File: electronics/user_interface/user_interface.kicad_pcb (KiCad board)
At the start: 2 copper layers, 2 parts

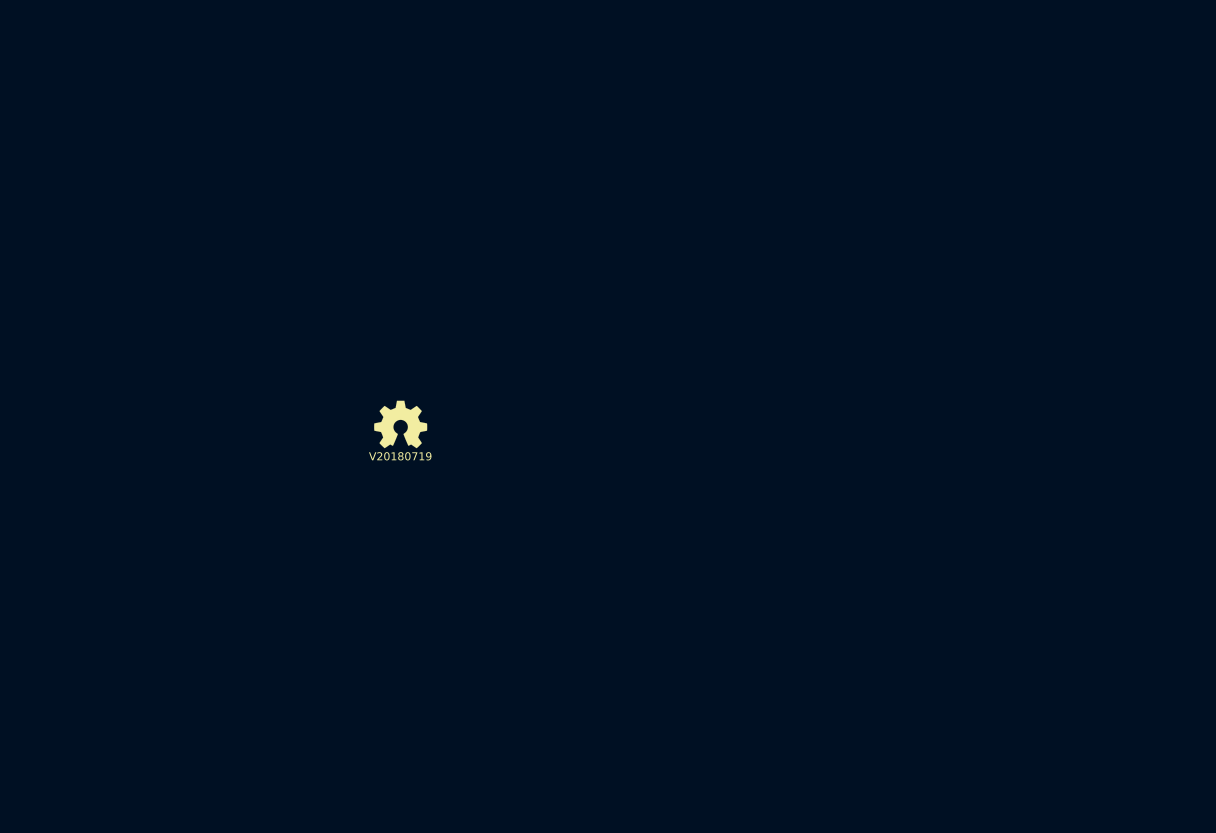
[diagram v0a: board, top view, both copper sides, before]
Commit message: board outline, input circuit layout
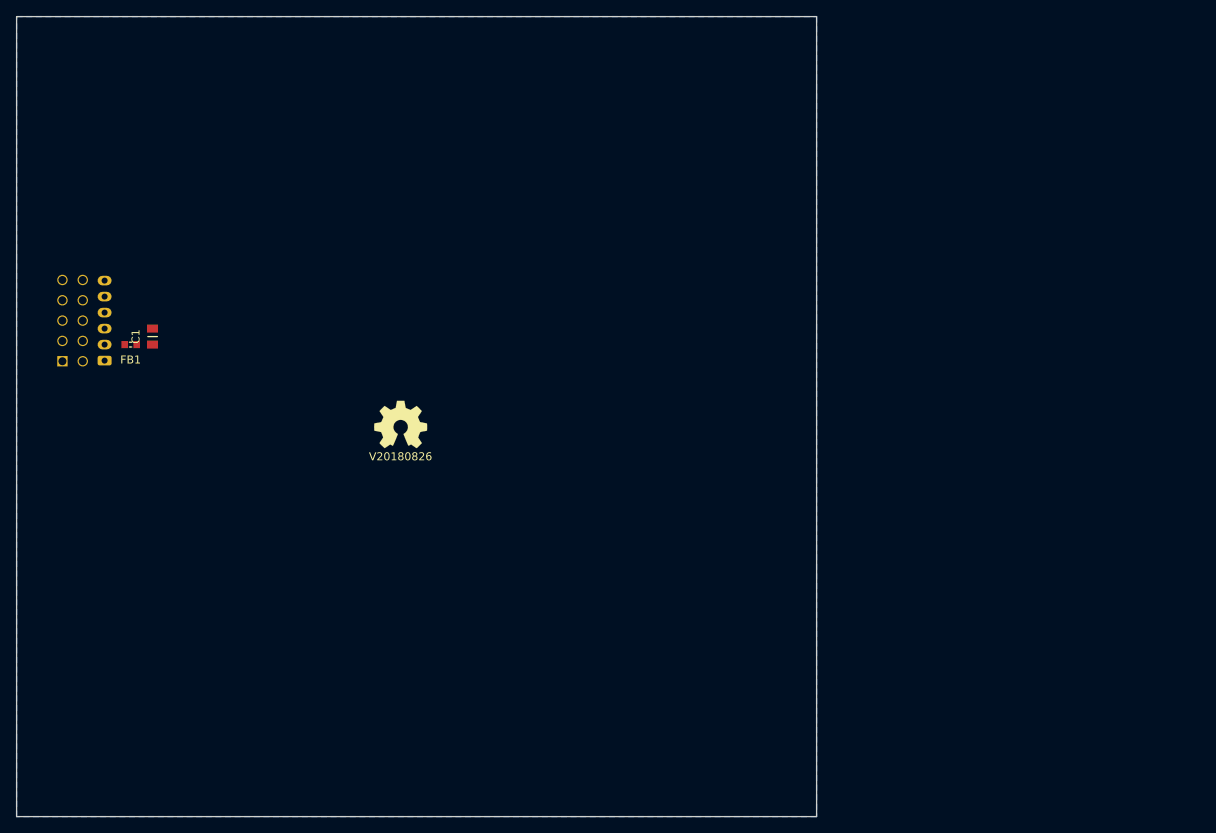
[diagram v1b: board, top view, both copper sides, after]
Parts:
- added C1: 10u, SquantorRcl:C_0805, F.Cu at (117.0, 90.0)
- added FB1: 600, SquantorRcl:L_0603, F.Cu at (114.2, 91.0)
- added J1: Conn_01x06, Connector_JST:JST_PH_S6B-PH-K_1x06_P2.00mm_Horizontal, B.Cu at (111.0, 93.0)
- added J2: Conn_02x05_Odd_Even, SquantorConnectors:Header-0254-2X05-H010, B.Cu at (107.0, 88.0)
- N2: value V20180719 -> V20180826
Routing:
- added copper zone on B.Cu, net /VSS
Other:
- board outline added: 100 x 100 mm

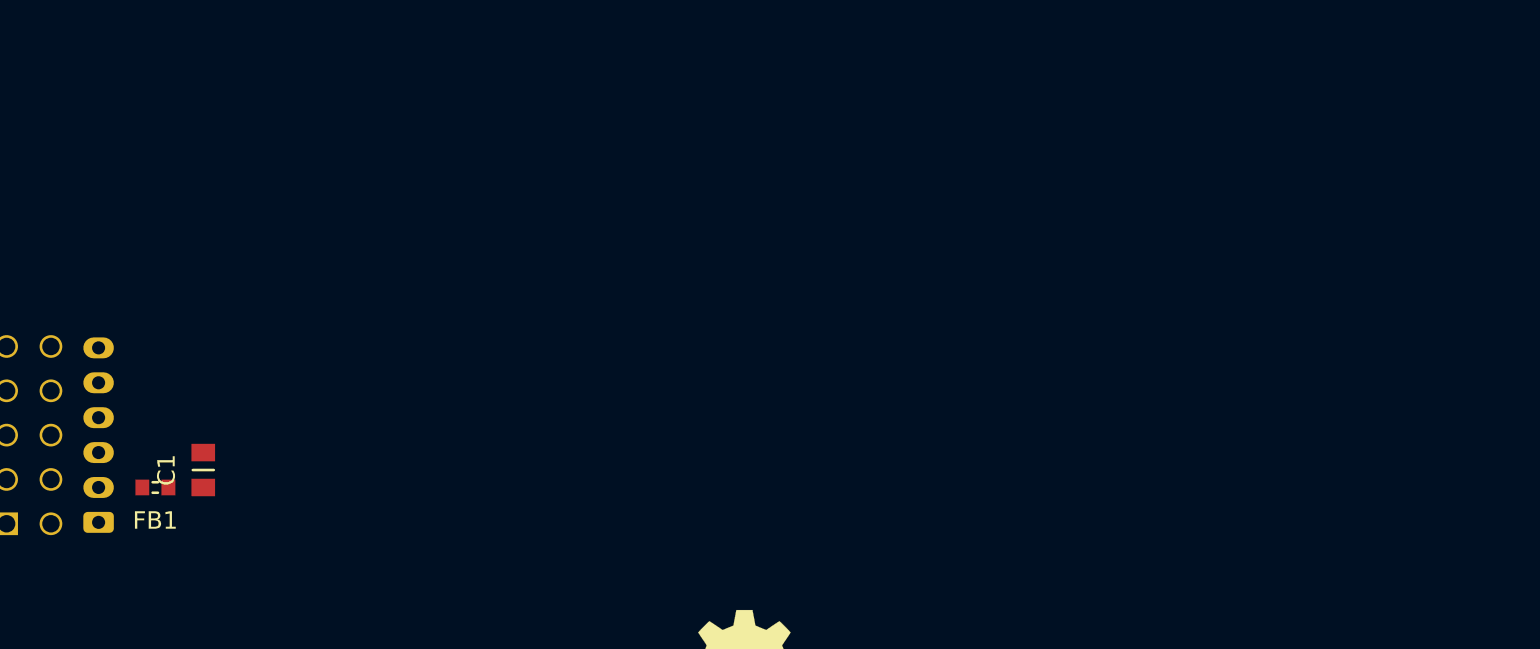
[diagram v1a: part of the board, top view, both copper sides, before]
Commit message: footprints assignment, minor layout positioning
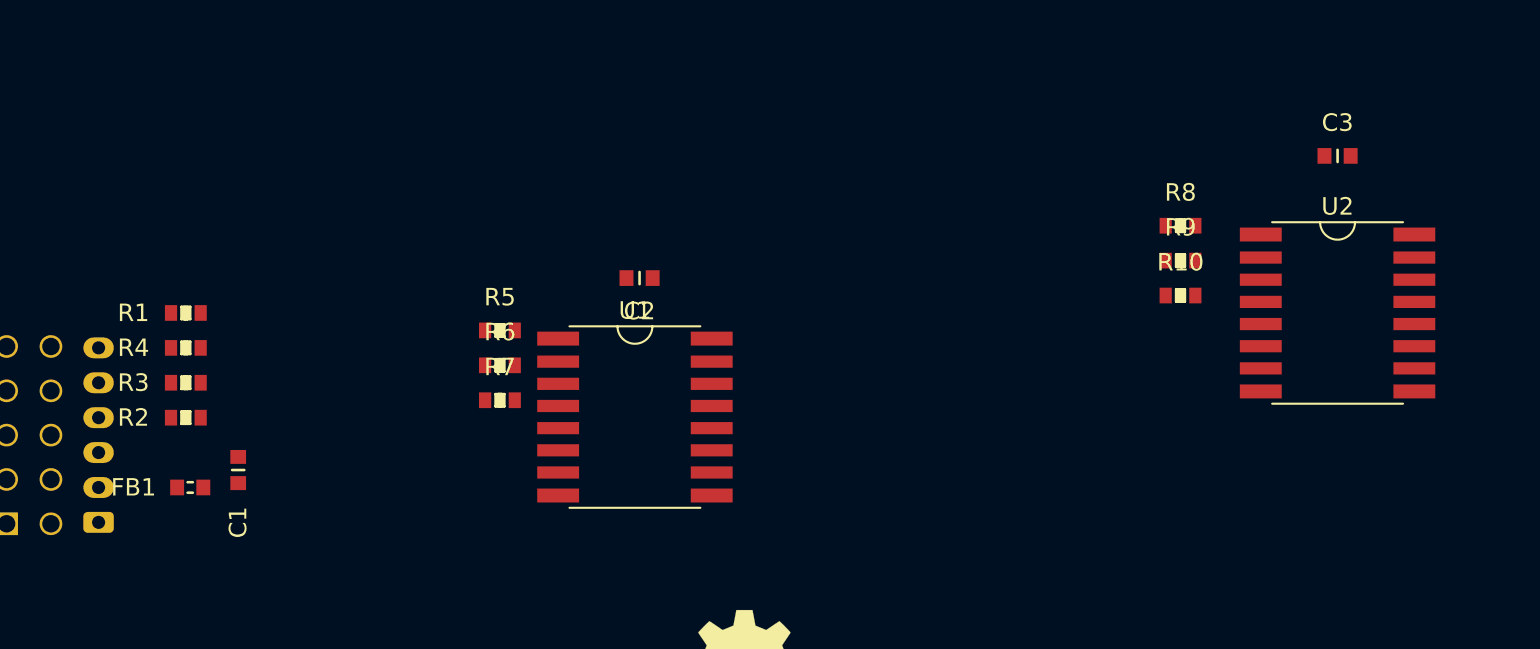
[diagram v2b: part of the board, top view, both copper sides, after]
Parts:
- added C2: 1u, SquantorRcl:C_0603, F.Cu at (142.0, 79.0)
- added C3: 1u, SquantorRcl:C_0603, F.Cu at (182.0, 72.0)
- added R1: 4.7K, SquantorRcl:R_0603_hand, F.Cu at (116.0, 81.0)
- added R10: 4.7K, SquantorRcl:R_0603_hand, F.Cu at (173.0, 80.0)
- added R2: 100, SquantorRcl:R_0603_hand, F.Cu at (116.0, 87.0)
- added R3: 100, SquantorRcl:R_0603_hand, F.Cu at (116.0, 85.0)
- added R4: 100, SquantorRcl:R_0603_hand, F.Cu at (116.0, 83.0)
- added R5: 4.7K, SquantorRcl:R_0603_hand, F.Cu at (134.0, 82.0)
- added R6: 4.7K, SquantorRcl:R_0603_hand, F.Cu at (134.0, 84.0)
- added R7: 4.7K, SquantorRcl:R_0603_hand, F.Cu at (134.0, 86.0)
- added R8: 4.7K, SquantorRcl:R_0603_hand, F.Cu at (173.0, 76.0)
- added R9: 4.7K, SquantorRcl:R_0603_hand, F.Cu at (173.0, 78.0)
- added U1: PCF8574, SquantorIC:SOT162-1-NXP, F.Cu at (141.7, 87.0)
- added U2: PCF8574, SquantorIC:SOT162-1-NXP, F.Cu at (182.0, 81.0)
- C1: footprint SquantorRcl:C_0805 -> SquantorRcl:C_0603
- moved C1 2.00 mm to (119.0, 90.0)
- moved FB1 2.00 mm to (116.2, 91.0)
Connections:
- net /!INT renamed /!INT_RAW
- net /SCL renamed /SCL_RAW
- net /SDA renamed /SDA_RAW

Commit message: updated date
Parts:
- N2: value V20180826 -> V20200514
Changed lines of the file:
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@@
       (effects (font (size 1 1) (thickness 0.15)))
     )
-    (fp_text value V20180826 (at 0 0) (layer F.SilkS)
+    (fp_text value V20200514 (at 0 0) (layer F.SilkS)
       (effects (font (size 1 1) (thickness 0.15)))
     )

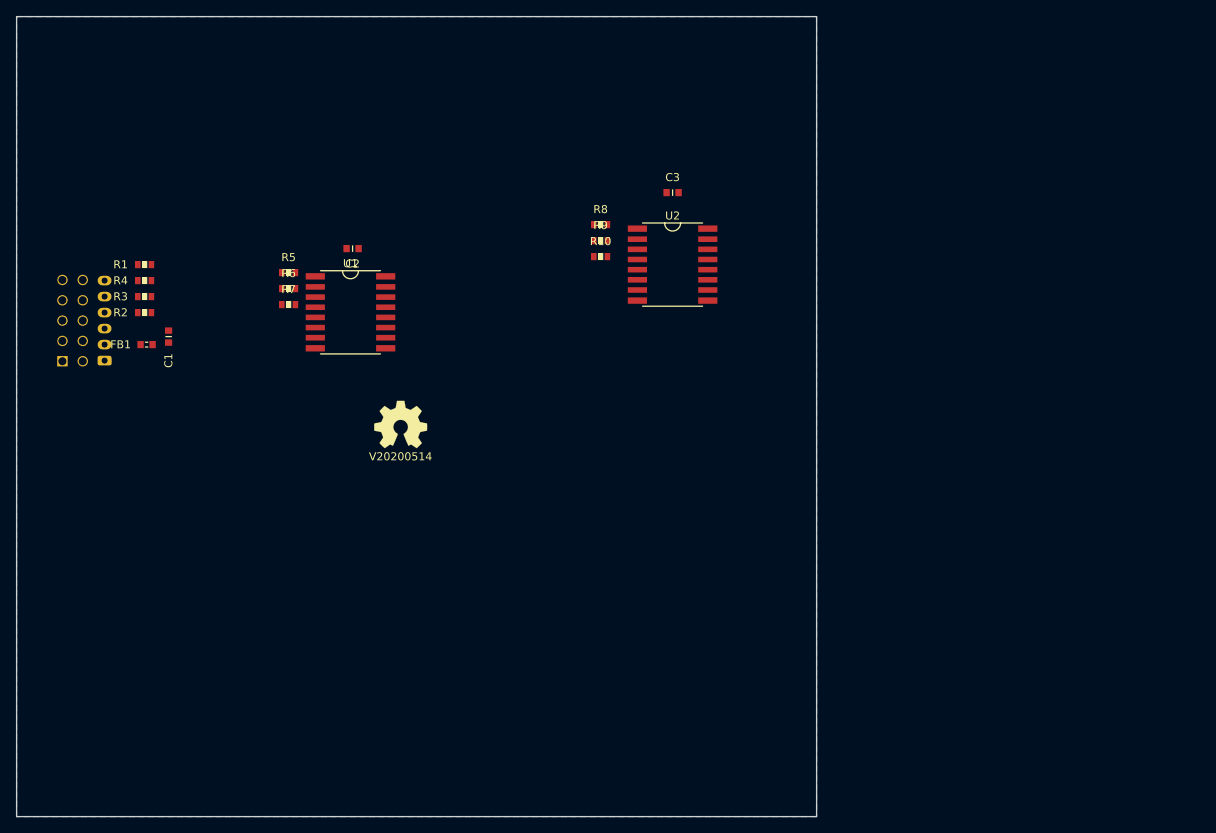
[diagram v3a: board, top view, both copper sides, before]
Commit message: added mounting holes, some silk moves
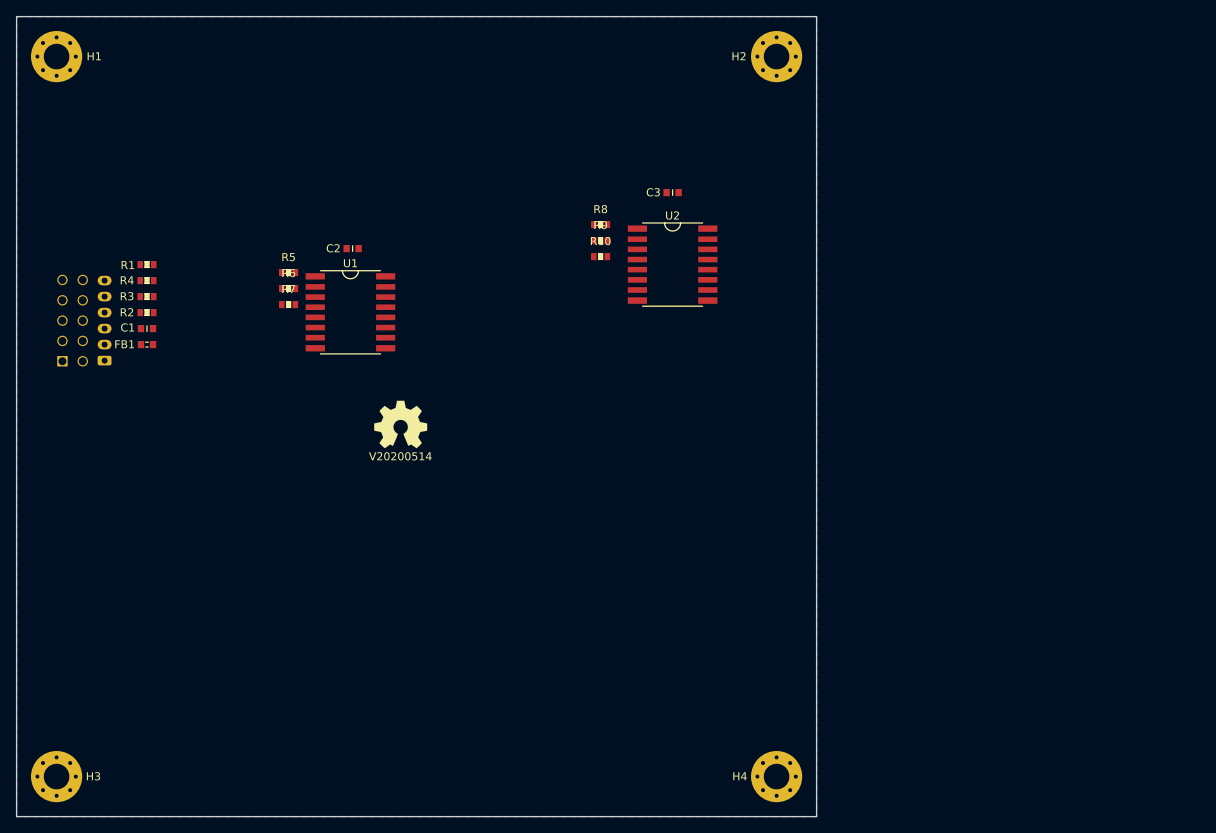
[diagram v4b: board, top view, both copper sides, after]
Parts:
- added H1: M3, MountingHole:MountingHole_3.2mm_M3_Pad_Via, F.Cu at (105.0, 55.0)
- added H2: M3, MountingHole:MountingHole_3.2mm_M3_Pad_Via, F.Cu at (195.0, 55.0)
- added H3: M3, MountingHole:MountingHole_3.2mm_M3_Pad_Via, F.Cu at (105.0, 145.0)
- added H4: M3, MountingHole:MountingHole_3.2mm_M3_Pad_Via, F.Cu at (195.0, 145.0)
- moved C1 2.88 mm to (116.3, 89.0), turned to 180 degrees
- moved R1 0.30 mm to (116.3, 81.0)
- moved R2 0.30 mm to (116.3, 87.0)
- moved R3 0.30 mm to (116.3, 85.0)
- moved R4 0.30 mm to (116.3, 83.0)

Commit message: added 3 switches extra to schematic
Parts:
- added C4: 1u, SquantorRcl:C_0603, F.Cu at (134.2, 114.4)
- added D1: RB521S-30, SquantorDiodes:SOD-523, F.Cu at (129.9, 119.4)
- added R11: TBD, SquantorRcl:R_0603_hand, F.Cu at (130.3, 114.5)
- added R12: TBD, SquantorRcl:R_0603_hand, F.Cu at (130.3, 117.0)
- added S1: Cherry Blue, MX_Only:MXOnly-1U-NoLED, F.Cu at (134.4, 131.7)
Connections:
- net Net-(U2-Pad5) renamed /Button_01
- net Net-(U2-Pad6) renamed /Button_02
- net Net-(U2-Pad7) renamed /Button_03
- U2 pad 4: Net-(U2-Pad4) -> /Button_00

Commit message: minor silk and layout
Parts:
- added C5: 100n, SquantorRcl:C_0603, F.Cu at (114.0, 139.0)
- added C6: 100n, SquantorRcl:C_0603, F.Cu at (158.0, 113.0)
- added C7: 100n, SquantorRcl:C_0603, F.Cu at (158.0, 133.0)
- added D2: RB521S-30, SquantorDiodes:SOD-523, F.Cu at (114.0, 137.0)
- added D3: RB521S-30, SquantorDiodes:SOD-523, F.Cu at (158.0, 115.0)
- added D4: RB521S-30, SquantorDiodes:SOD-523, F.Cu at (158.0, 135.0)
- added R13: TBD, SquantorRcl:R_0603_hand, F.Cu at (113.8, 133.0)
- added R14: TBD, SquantorRcl:R_0603_hand, F.Cu at (158.0, 119.0)
- added R15: TBD, SquantorRcl:R_0603_hand, F.Cu at (158.0, 139.0)
- added R16: TBD, SquantorRcl:R_0603_hand, F.Cu at (113.8, 135.0)
- added R17: TBD, SquantorRcl:R_0603_hand, F.Cu at (158.0, 117.0)
- added R18: TBD, SquantorRcl:R_0603_hand, F.Cu at (158.0, 137.0)
- added S2: Cherry Blue, MX_Only:MXOnly-1U-NoLED, F.Cu at (126.0, 136.0)
- added S3: Cherry Blue, MX_Only:MXOnly-1U-NoLED, F.Cu at (146.0, 116.0)
- added S4: Cherry Blue, MX_Only:MXOnly-1U-NoLED, F.Cu at (146.0, 136.0)
- C4: value 1u -> 100n
- moved N1 98.1 mm to (238.0, 62.0)
- moved R7 23.4 mm to (152.0, 71.0), turned to 180 degrees
- moved R6 21.1 mm to (152.0, 73.0), turned to 180 degrees
- moved C4 20.7 mm to (114.0, 119.0)
- moved R5 19.3 mm to (152.0, 75.0), turned to 180 degrees
- moved S1 17.8 mm to (126.0, 116.0), turned to 90 degrees
- moved C1 17.6 mm to (128.4, 76.2)
- moved FB1 17.6 mm to (128.4, 78.2)
- moved R1 17.6 mm to (128.4, 68.2)
- moved R2 17.6 mm to (128.4, 74.2), turned to 180 degrees
- moved R3 17.6 mm to (128.4, 72.2)
- moved R4 17.6 mm to (128.4, 70.2)
- moved J1 17.6 mm to (123.1, 80.2)
- moved J2 17.6 mm to (119.1, 75.2)
- moved R10 17.5 mm to (188.0, 71.0), turned to 180 degrees
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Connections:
- C4 pad 1: /VSS -> /Button_00
- C4 pad 2: /Button_00 -> /VSS
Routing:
- net /VDD: track 0.00 -> 14.6 mm, vias 0 -> 2
- net /VSS: track 0.00 -> 13.6 mm
- net Net-(D1-Pad2): track 0.00 -> 10.3 mm
- net /SDA_RAW: track 0.00 -> 7.59 mm
- net /VDD_RAW: track 0.00 -> 7.47 mm
- net /SCL_RAW: track 0.00 -> 7.37 mm
- net /!INT_RAW: track 0.00 -> 7.21 mm
- net /Button_00: track 0.00 -> 4.08 mm
- net /!INT: track 0.00 -> 2.00 mm
